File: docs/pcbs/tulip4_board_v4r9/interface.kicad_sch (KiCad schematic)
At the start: 34 parts, among them J1 217179-0001, J1 XF2M-4015-1A, J2 1734709-4, J4 SJ2-35863B1, J6 SJ2-35863B1, U2 USBLC6-2SC6, U3 FT231XS, U5 MIC2005A-2YM5-TR, U6 H11L1SR2M

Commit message: Progress routing
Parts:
- renumbered C3 to C?, C1 to C?, C2 to C?, C5 to C?, C23 to C?, C4 to C?, FB1 to FB?, J1 to J?, R1 to R?, R4 to R?, R3 to R?, R2 to R?, U3 to U?, U2 to U?
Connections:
- net +5V: no longer U?.5 (VBUS)
- net +5VL: now also U?.5 (VBUS)
- no-connect marks 17 -> 18

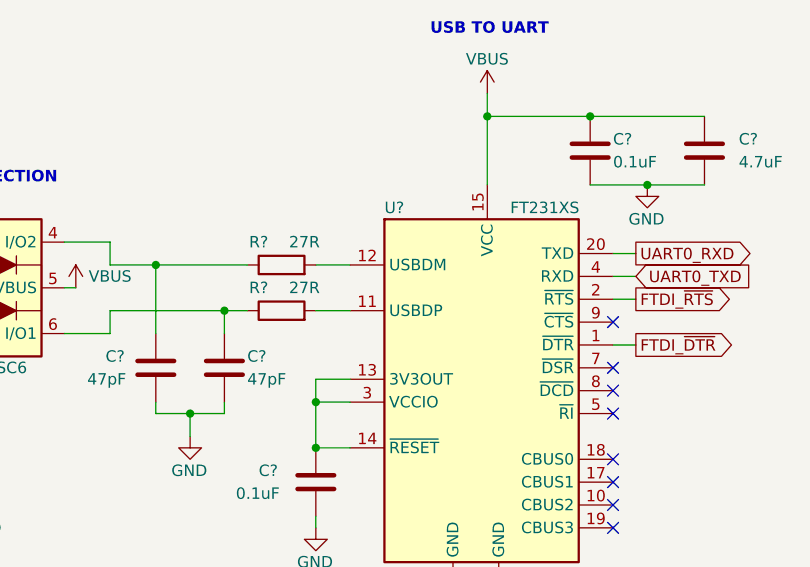
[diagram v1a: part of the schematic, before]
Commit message: V4R9A: USB, Audio circuit fix. Updated component part #s.
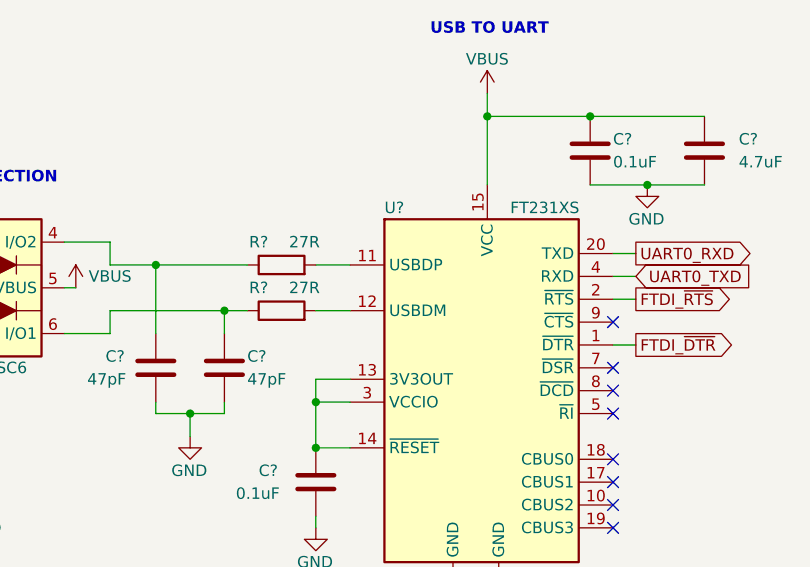
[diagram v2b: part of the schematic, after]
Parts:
- R13: Part # CR0805-FX-4703ELF -> CR0805-FX-4700ELF; Supplier 1 # 652-CR0805FX-4703ELF -> 652-CR0805FX-4700ELF; Supplier 2 # 118-CMP1206-FX-4703ELFCT-ND -> CR0805-FX-4700ELFCT-ND
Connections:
- net at U?.11 (USBDP): now also R?.2; no longer R?.2
- net at U?.12 (USBDM): now also R?.2; no longer R?.2
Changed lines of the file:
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@@
     (fill (type none))
+  )
+  (text_box ""
+    (at 195.58 92.71 0) (size 0 0)
+    (stroke (width 0) (type default) (color 194 0 0 1))
+    (fill (type none))
+    (effects (font (size 1.27 1.27)) (justify left top))
   )
   (text "USB TO UART" (at 133.35 27.94 0)
@@
       (effects (font (size 1.27 1.27)) hide)
     )
-    (property "Part #" "CR0805-FX-4703ELF" (at 226.06 132.08 0)
+    (property "Part #" "CR0805-FX-4700ELF" (at 226.06 132.08 0)
       (effects (font (size 1.27 1.27)) hide)
     )
@@
       (effects (font (size 1.27 1.27)) hide)
     )
-    (property "Supplier 1 #" "652-CR0805FX-4703ELF" (at 231.14 132.08 0)
+    (property "Supplier 1 #" "652-CR0805FX-4700ELF" (at 231.14 132.08 0)
       (effects (font (size 1.27 1.27)) hide)
     )
@@
       (effects (font (size 1.27 1.27)) hide)
     )
-    (property "Supplier 2 #" "118-CMP1206-FX-4703ELFCT-ND" (at 236.22 132.08 0)
-      (effects (font (size 1.27 1.27)) hide)
-    )
+    (property "Supplier 2 #" "CR0805-FX-4700ELFCT-ND" (at 236.22 132.08 0)
+      (effects (font (size 1.27 1.27)) hide)
+    )
